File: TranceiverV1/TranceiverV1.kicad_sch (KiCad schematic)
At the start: 8 parts, among them J1 Conn_01x02_Socket, J2 Conn_01x02_Pin, J3 Conn_01x03_Socket, J4 Conn_01x03_Pin, M1 Motor_Servo, SW1 SW_Push, U1 ESP32-WROOM-32E, U2 ESP32-WROOM-32E

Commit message: added first rough iteration of shcematic and pcb for transceiver
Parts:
- J1: footprint Connector_PinHeader_2.54mm:PinHeader_1x02_P2.54mm_Vertical -> Connector_PinHeader_2.54mm:PinHeader_1x02_P2.54mm_Horizontal
- U1: footprint RF_Module:ESP32-WROOM-32D -> ArduinoXIAO:MODULE_102010388
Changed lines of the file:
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@@
 			)
 		)
-		(property "Footprint" "RF_Module:ESP32-WROOM-32D"
+		(property "Footprint" "ArduinoXIAO:MODULE_102010388"
 			(at 78.74 124.46 0)
 			(effects
@@
 			)
 		)
-		(property "Footprint" "Connector_PinHeader_2.54mm:PinHeader_1x02_P2.54mm_Vertical"
+		(property "Footprint" "Connector_PinHeader_2.54mm:PinHeader_1x02_P2.54mm_Horizontal"
 			(at 90.17 118.11 0)
 			(effects

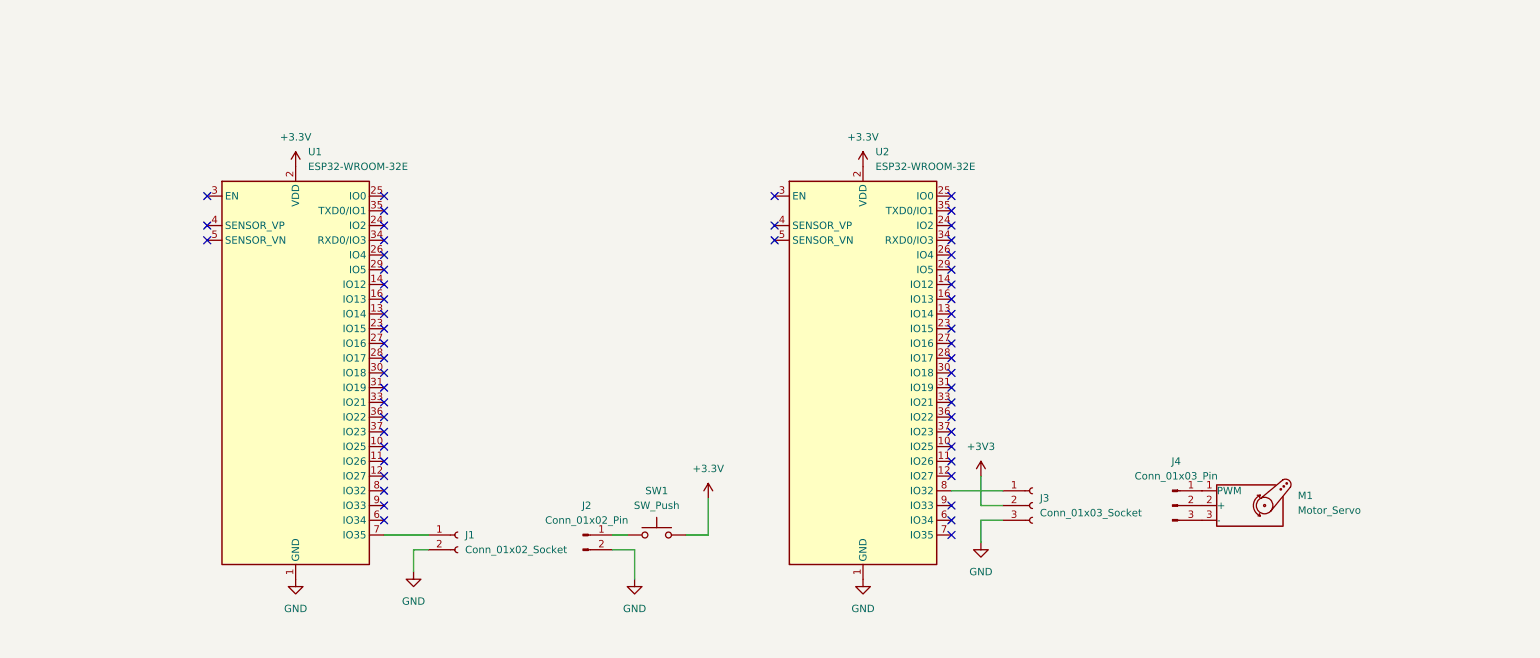
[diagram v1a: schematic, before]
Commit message: arduino XIAO footprint and symbol added
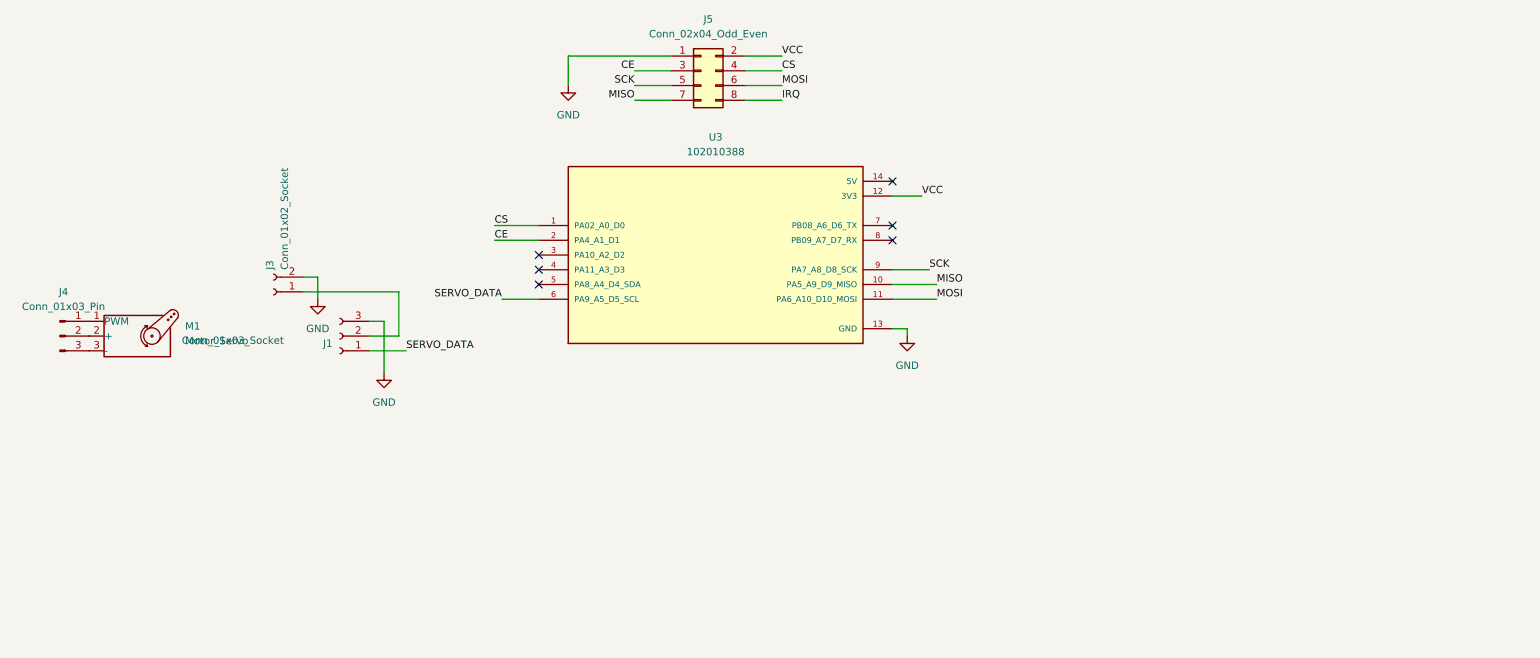
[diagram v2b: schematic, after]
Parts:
- removed J1: Conn_01x02_Socket, Connector_PinHeader_2.54mm:PinHeader_1x02_P2.54mm_Horizontal, symbol Connector:Conn_01x02_Socket
- removed J2: Conn_01x02_Pin, symbol Connector:Conn_01x02_Pin
- removed J3: Conn_01x03_Socket, Connector_PinHeader_2.54mm:PinHeader_1x03_P2.54mm_Vertical, symbol Connector:Conn_01x03_Socket
- removed SW1: SW_Push, symbol Switch:SW_Push
- removed U1: ESP32-WROOM-32E, ArduinoXIAO:MODULE_102010388, symbol RF_Module:ESP32-WROOM-32E
- removed U2: ESP32-WROOM-32E, RF_Module:ESP32-WROOM-32D, symbol RF_Module:ESP32-WROOM-32E
- added J1: Conn_01x03_Socket, Connector_PinHeader_2.54mm:PinHeader_1x03_P2.54mm_Vertical, symbol Connector:Conn_01x03_Socket
- added J3: Conn_01x02_Socket, Connector_PinHeader_2.54mm:PinHeader_1x02_P2.54mm_Vertical, symbol Connector:Conn_01x02_Socket
- added J5: Conn_02x04_Odd_Even, Connector_PinHeader_2.54mm:PinHeader_2x04_P2.54mm_Vertical, symbol Connector_Generic:Conn_02x04_Odd_Even
- added U3: 102010388, ArduinoXIAO:MODULE_102010388, symbol 102010388:102010388
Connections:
- net GND: now also J1.3 (Pin_3), J3.2 (Pin_2), J5.1 (Pin_1), U3.13 (GND)
- new net: J1.2 (Pin_2), J3.1 (Pin_1)
- new net CE: J5.3 (Pin_3), U3.2 (PA4_A1_D1)
- new net CS: J5.4 (Pin_4), U3.1 (PA02_A0_D0)
- new net IRQ: J5.8 (Pin_8)
- new net MISO: J5.7 (Pin_7), U3.10 (PA5_A9_D9_MISO)
- new net MOSI: J5.6 (Pin_6), U3.11 (PA6_A10_D10_MOSI)
- new net SCK: J5.5 (Pin_5), U3.9 (PA7_A8_D8_SCK)
- new net SERVO_DATA: J1.1 (Pin_1), U3.6 (PA9_A5_D5_SCL)
- new net VCC: J5.2 (Pin_2), U3.12 (3V3)
- no-connect marks 52 -> 6
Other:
- moved on the sheet: J4, M1

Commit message: designed first iteration of pcb
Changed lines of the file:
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@@
+	(wire
+		(pts
+			(xy 139.7 43.18) (xy 146.05 43.18)
+		)
+		(stroke
+			(width 0)
+			(type default)
+		)
+	)
 	(wire
 		(pts
@@
 	(wire
 		(pts
-			(xy 146.05 43.18) (xy 139.7 43.18)
-		)
-		(stroke
-			(width 0)
-			(type default)
-		)
-	)
-	(wire
-		(pts
 			(xy 120.65 43.18) (xy 127 43.18)
 		)
@@
 	(label "CE"
 		(at 96.52 67.31 0)
-		(effects
-			(font
-				(size 1.27 1.27)
-			)
-			(justify left bottom)
-		)
-	)
-	(label "IRQ"
-		(at 146.05 43.18 0)
 		(effects
 			(font
@@
 		)
 	)
+	(label "IRQ"
+		(at 146.05 43.18 0)
+		(effects
+			(font
+				(size 1.27 1.27)
+			)
+			(justify left bottom)
+		)
+	)

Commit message: updated schematic for pcb iteration
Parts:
- removed J5: Conn_02x04_Odd_Even, Connector_PinHeader_2.54mm:PinHeader_2x04_P2.54mm_Vertical, symbol Connector_Generic:Conn_02x04_Odd_Even
- added C1, C5: 100u, symbol Device:C
- added C3: 10u, symbol Device:C
- added C4: 22u, symbol Device:C
- added D1, D2: LED, LED_THT:LED_D5.0mm, symbol Device:LED
- added D3: D_Schottky, symbol Device:D_Schottky
- added R1, R3: 1k, symbol Device:R_US
- added R2, R4: 1k, Resistor_THT:R_Axial_DIN0204_L3.6mm_D1.6mm_P2.54mm_Vertical, symbol Device:R_US
- added S1: TS02-66-50-BK-100-LCR-D, TS02_66_50_BK_100_LCR_D_Folder:SW_TS02-66-50-BK-100-LCR-D, symbol TS02-66-50-BK-100-LCR-D:TS02-66-50-BK-100-LCR-D
- added SW1: SW_Push_Open, Button_Switch_THT:SW_PUSH_1P1T_6x3.5mm_H5.0_APEM_MJTP1250, symbol Switch:SW_Push_Open
- added U1: NRF24L01_, RF_Module:nRF24L01_Breakout, symbol NRF24L01_:NRF24L01_
- added U2: LD0186D2T50TR, Package_TO_SOT_SMD:TO-263-2, symbol Regulator_Linear:LD0186D2T50TR
- J3: value Conn_01x02_Socket -> Battery
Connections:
- net CE: now also U1.P$3 (CE)
- net GND: now also C1.2, C3.2, C4.2, C5.2, D1.1 (K), D2.1 (K), S1.2, U1.P$1 (GND), U2.1 (ADJ/GND)
- net IRQ: now also U1.P$8 (IRQ)
- net MISO: now also U1.P$7 (MISO)
- net MOSI: now also U1.P$6 (MOSI)
- net SCK: now also U1.P$5 (SCK)
- net VCC: now also C5.1, R1.1, U1.P$2 (VCC)
- net 5V_IN: now reaches U3.14 (5V)
- net 5V_IN: now also R3.2
- net DIG_IN: now reaches U3.3 (PA10_A2_D2)
- net DIG_IN: now also R1.2, S1.3
- net LED_ON1: now reaches U3.4 (PA11_A3_D3)
- net LED_ON1: now also R2.1
- net LED_ON2: now reaches U3.5 (PA8_A4_D4_SDA)
- net LED_ON2: now also R4.1
- net at J3.1 (Pin_1): now also SW1.1 (A); no longer J1.2 (Pin_2)
- net CS renamed CSN
- net CSN: now also U1.P$4 (CSN)
- new net: D2.2 (A), R2.2
- new net: D3.1 (K), R3.1
- new net: D1.2 (A), R4.2
- new net 5V: C4.1, D3.2 (A), U2.2 (OUT)
- new net Regulator_In: C1.1, C3.1, J1.2 (Pin_2), SW1.2 (B), U2.3 (IN)
- no-connect marks 6 -> 5
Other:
- moved on the sheet: J1, J3, J4, M1

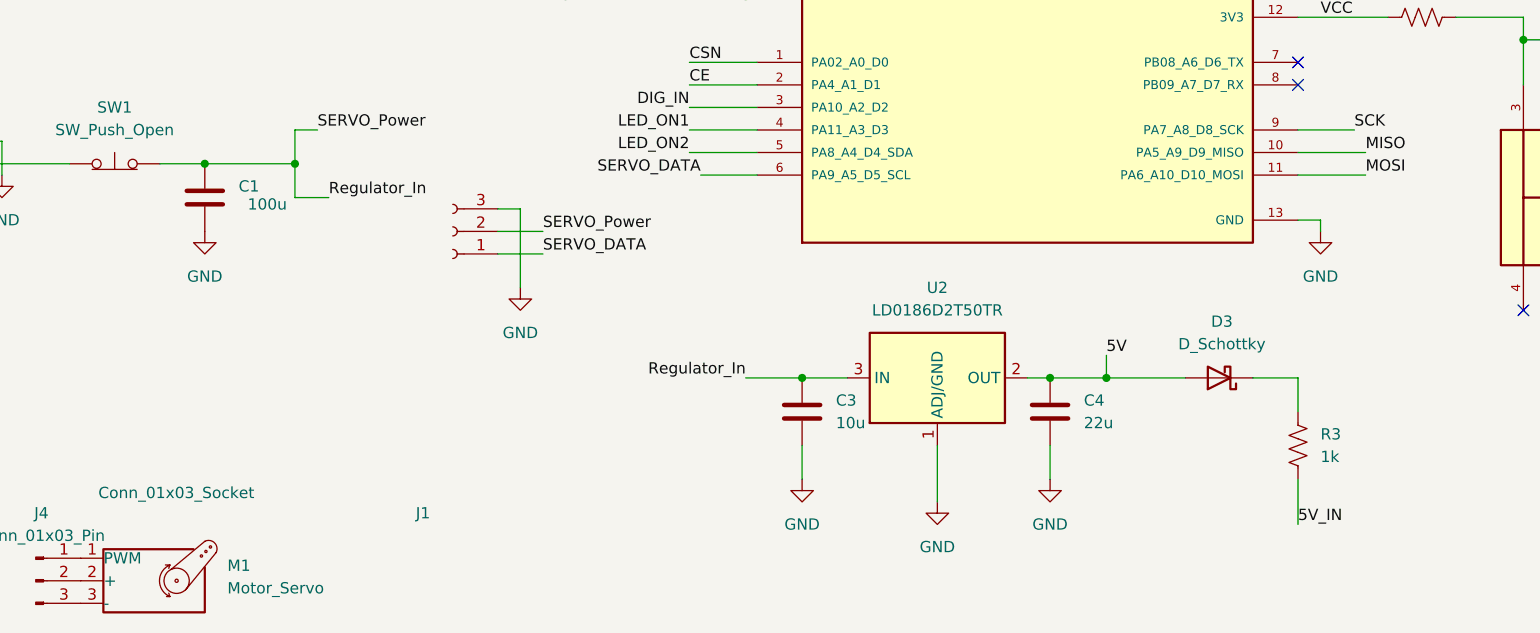
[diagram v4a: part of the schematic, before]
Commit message: made first iteration of pcb with all footprints tht
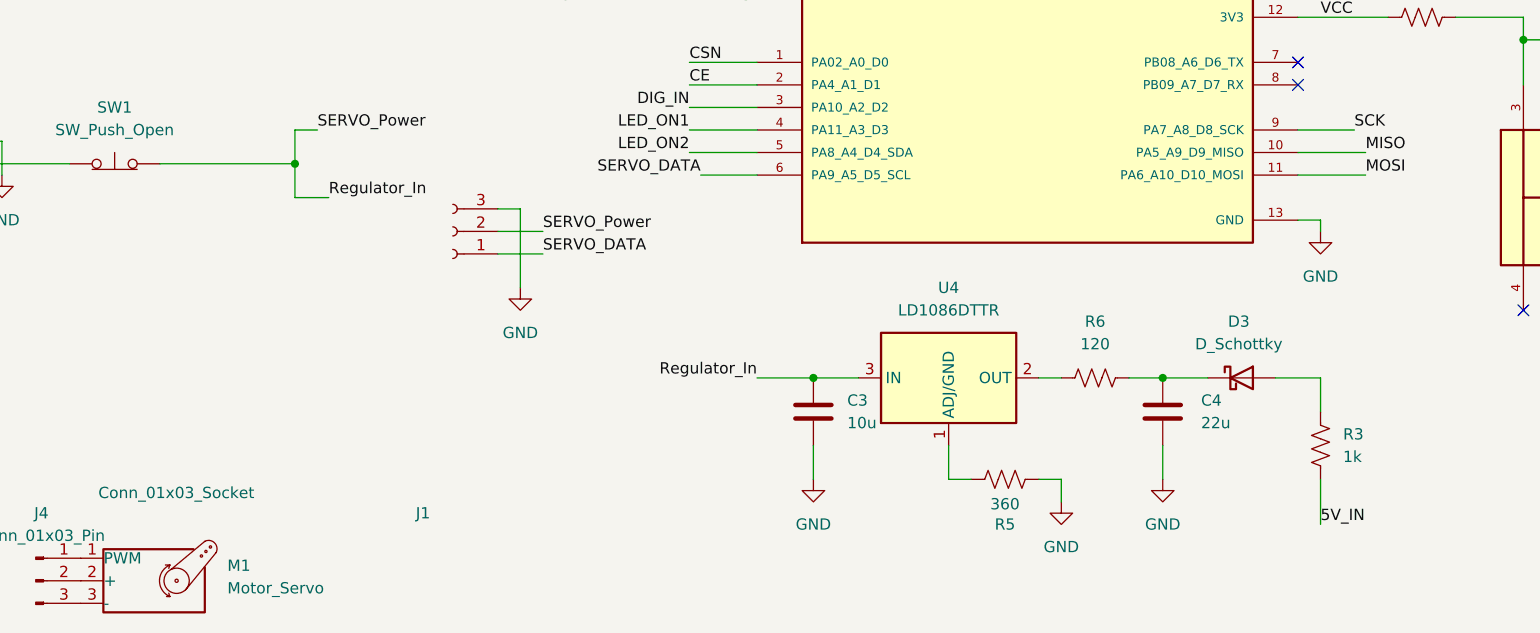
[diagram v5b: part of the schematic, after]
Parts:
- removed C1: 100u, symbol Device:C
- removed U2: LD0186D2T50TR, Package_TO_SOT_SMD:TO-263-2, symbol Regulator_Linear:LD0186D2T50TR
- added R5: 360, Resistor_THT:R_Axial_DIN0204_L3.6mm_D1.6mm_P2.54mm_Vertical, symbol Device:R_US
- added R6: 120, Resistor_THT:R_Axial_DIN0204_L3.6mm_D1.6mm_P2.54mm_Vertical, symbol Device:R_US
- added U4: LD1086DTTR, Package_TO_SOT_SMD:TO-252-2, symbol Regulator_Linear:LD1086DTTR
- C3, C4, C5: footprint (none) -> Capacitor_THT:C_Axial_L3.8mm_D2.6mm_P7.50mm_Horizontal
- D3: footprint (none) -> Diode_THT:D_T-1_P2.54mm_Vertical_AnodeUp
- R1, R3: footprint (none) -> Resistor_THT:R_Axial_DIN0204_L3.6mm_D1.6mm_P2.54mm_Vertical
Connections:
- net GND: now also R5.1
- net Regulator_In: now also U4.3 (IN)
- net at R3.1: now also D3.2 (A); no longer D3.1 (K)
- net 5V: no longer names the net of C4.1
- net 5V: now also D3.1 (K), R6.2; no longer D3.2 (A)
- new net: R5.2, U4.1 (ADJ/GND)
- new net: R6.1, U4.2 (OUT)
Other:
- moved on the sheet: C3, C4, D3, R3
